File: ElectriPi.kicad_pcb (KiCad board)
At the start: 2 copper layers, 65 x 56 mm, 59 parts, among them IC2 TPS51397ARJER, J1 282837-2, J3 JST XH 01x02, J4 282837-2, J6 Raspberry_Pi_2_3, Q1 SiA471DJ, U1 LM73100, U2 COOLING, U3 TVS0500DRV, U4 LM73100

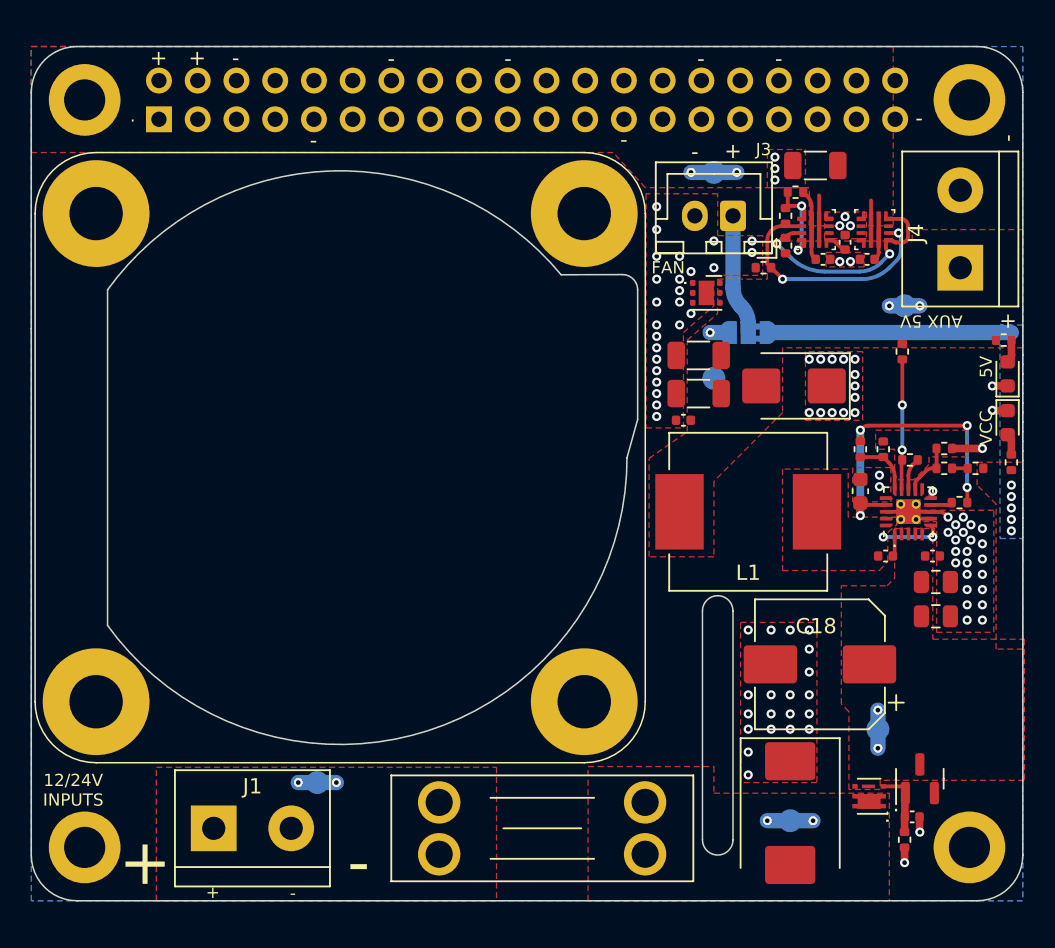
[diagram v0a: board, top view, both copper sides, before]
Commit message: Change to 40 pin passthrough header
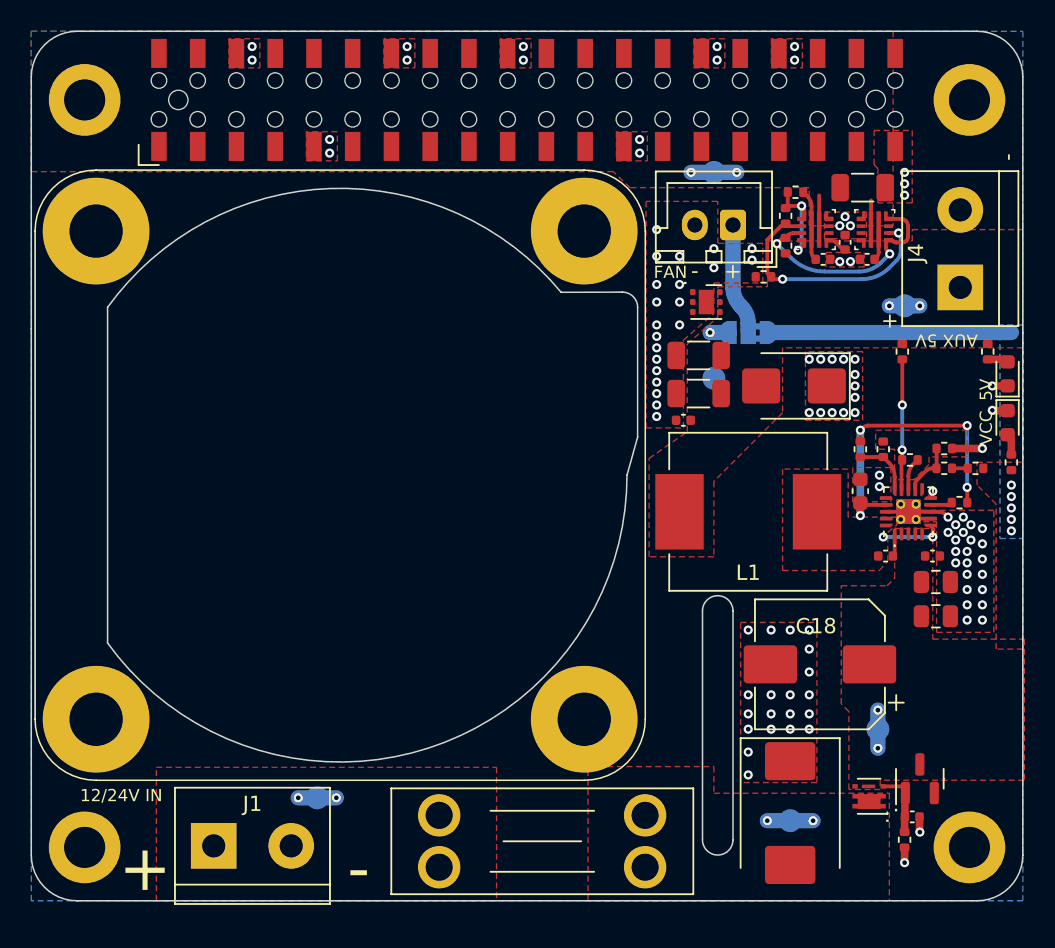
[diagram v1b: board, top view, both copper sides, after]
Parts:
- J6: value Raspberry_Pi_2_3 -> Raspberry_Pi_Header; footprint Connector_PinSocket_2.54mm:PinSocket_2x20_P2.54mm_Vertical -> PI_GPIO_PASSTHROUGH:SSM-120-_-DV-BE; moved to F.Cu
- moved C12 3.42 mm to (139.8, 62.5), turned to 0 degrees
- moved R6 1.29 mm to (147.9, 73.2), turned to 90 degrees
- moved J4 1.29 mm to (146.2, 69.0)
- moved J1 1.15 mm to (97.2, 105.7)
- moved U2 1.15 mm to (105.5, 81.3)
- moved TP2 1.00 mm to (104.0, 102.5)
- moved F1 0.85 mm to (112.0, 103.7)
- moved J3 0.60 mm to (131.2, 65.0)
- moved R10 0.60 mm to (133.2, 68.3)
- moved U3 0.60 mm to (129.5, 70.0)
- turned J6 to 90 degrees
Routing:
- net Net-(J3-Pin_1): track 7.91 -> 7.31 mm
- net GND: vias 97 -> 107
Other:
- board size 65 x 56 mm -> 65 x 57 mm
- board text added: "12/24V IN"
- board text removed: "12/24V INPUTS"

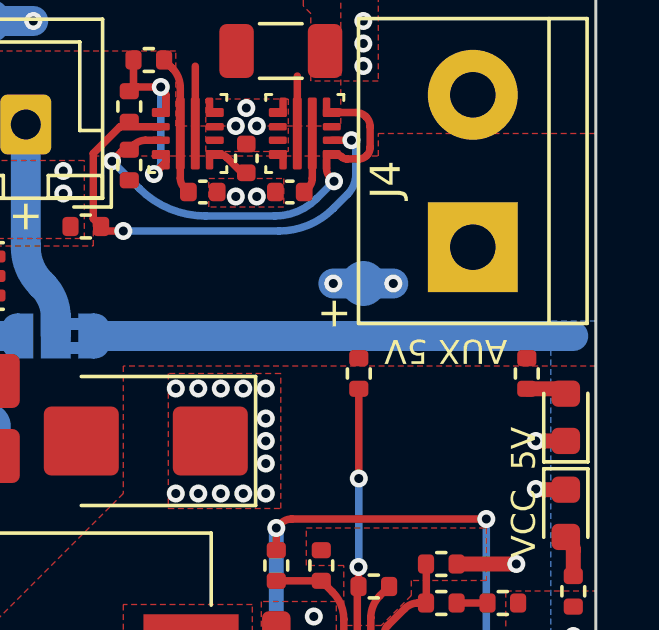
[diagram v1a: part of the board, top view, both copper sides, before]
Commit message: Change silk and test point position. Update manufacturing outputs. Header product number not yet specified
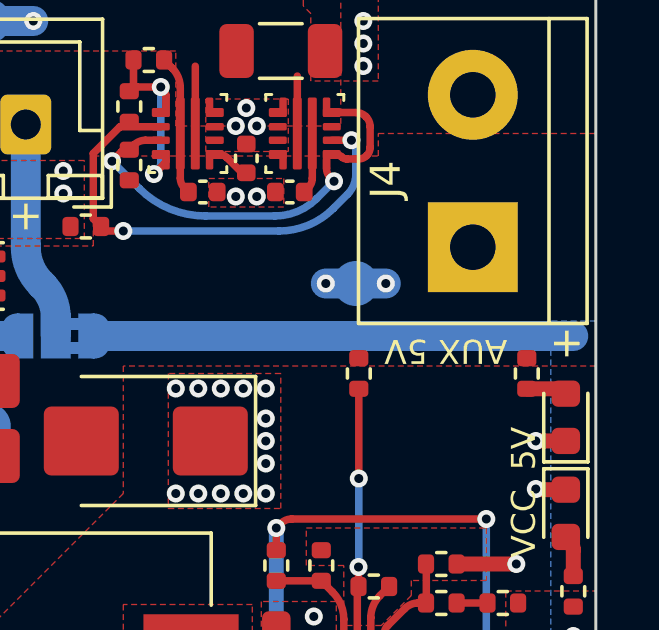
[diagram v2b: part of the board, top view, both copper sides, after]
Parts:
- moved TP1 0.25 mm to (142.2, 70.2)
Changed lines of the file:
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@@
 		(pad_to_mask_clearance 0)
 		(allow_soldermask_bridges_in_footprints no)
-		(aux_axis_origin 85.25 53.25)
-		(grid_origin 85.25 53.25)
+		(aux_axis_origin 85.25 52.25)
+		(grid_origin 85.25 52.249996)
 		(pcbplotparams
 			(layerselection 0x00010fe_ffffffff)
@@
 		(tags "capacitor")
 		(property "Reference" "C12"
-			(at 0 -1.85 360)
+			(at 0 -1.85 0)
 			(layer "F.SilkS")
 			(hide yes)
@@
 		)
 		(property "Value" "100uF"
-			(at 0 1.85 360)
+			(at 0 1.85 0)
 			(layer "F.Fab")
 			(effects
@@
 		)
 		(property "Footprint" "Capacitor_SMD:C_1206_3216Metric"
-			(at 0 0 360)
+			(at 0 0 0)
 			(layer "F.Fab")
 			(hide yes)
@@
 		)
 		(property "Datasheet" ""
-			(at 0 0 360)
+			(at 0 0 0)
 			(layer "F.Fab")
 			(hide yes)
@@
 		)
 		(property "Description" ""
-			(at 0 0 360)
+			(at 0 0 0)
 			(layer "F.Fab")
 			(hide yes)
@@
 		)
 		(property "DigiKey" "490-GRM31CR61A107MEA8KTR-ND"
-			(at 273.3 122.1 360)
+			(at 273.3 122.1 0)
 			(layer "F.Fab")
 			(hide yes)
@@
 		)
 		(property "LCSC" "C312983"
-			(at 273.3 122.1 360)
+			(at 273.3 122.1 0)
 			(layer "F.Fab")
 			(hide yes)
@@
 		)
 		(property "Mouser" "81-GRM31CR61A107MA8L"
-			(at 273.3 122.1 360)
+			(at 273.3 122.1 0)
 			(layer "F.Fab")
 			(hide yes)
@@
 		)
 		(fp_text user "${REFERENCE}"
-			(at 0 0 360)
+			(at 0 0 0)
 			(layer "F.Fab")
 			(effects
@@
 		)
 		(fp_text user "${REFERENCE}"
-			(at 1.27 24.13 360)
+			(at 1.27 24.13 0)
 			(layer "F.Fab")
 			(effects
@@
 		(tags "resistor")
 		(property "Reference" "R6"
-			(at 1.6 0.35 360)
+			(at 1.6 0.35 0)
 			(layer "F.SilkS")
 			(hide yes)
@@
 	(footprint "TestPoint:TestPoint_Pad_D1.5mm"
 		(layer "B.Cu")
-		(at 142.5 70.25)
+		(at 142.25 70.25)
 		(descr "SMD pad as test Point, diameter 1.5mm")
 		(tags "test point SMD pad")
@@
 	)
 	(gr_text "+"
-		(at 141.5 71.25 90)
+		(at 149.25 72.25 90)
 		(layer "F.SilkS")
 		(effects
@@
 	)
 	(via
-		(at 143.5 70.25)
+		(at 143.25 70.25)
 		(size 0.6)
 		(drill 0.3)
@@
 	)
 	(via
-		(at 141.5 70.25)
+		(at 141.25 70.25)
 		(size 0.6)
 		(drill 0.3)
@@
 	)
 	(segment
-		(start 141.5 70.25)
-		(end 143.5 70.25)
+		(start 141.25 70.25)
+		(end 143.25 70.25)
 		(width 1)
 		(layer "B.Cu")

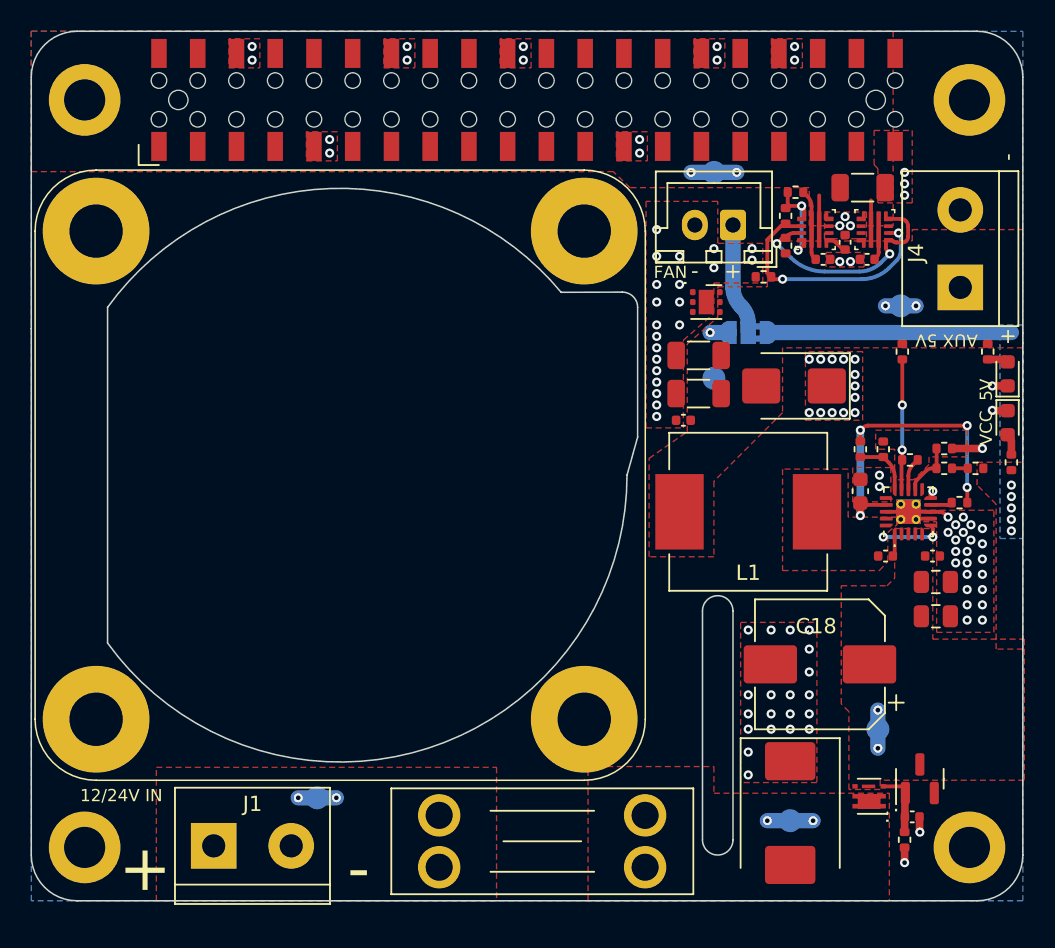
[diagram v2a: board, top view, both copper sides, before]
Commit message: V1.1 Updates
Moved status LEDs away from PCB edge.
Moved and modified AUX 5V label.
Changed screw terminals to JST XH.
Added SMD Header LCSC number.
Added 5mm silkscreen for QR Code
Removed silkscreen border for 4010 fan.
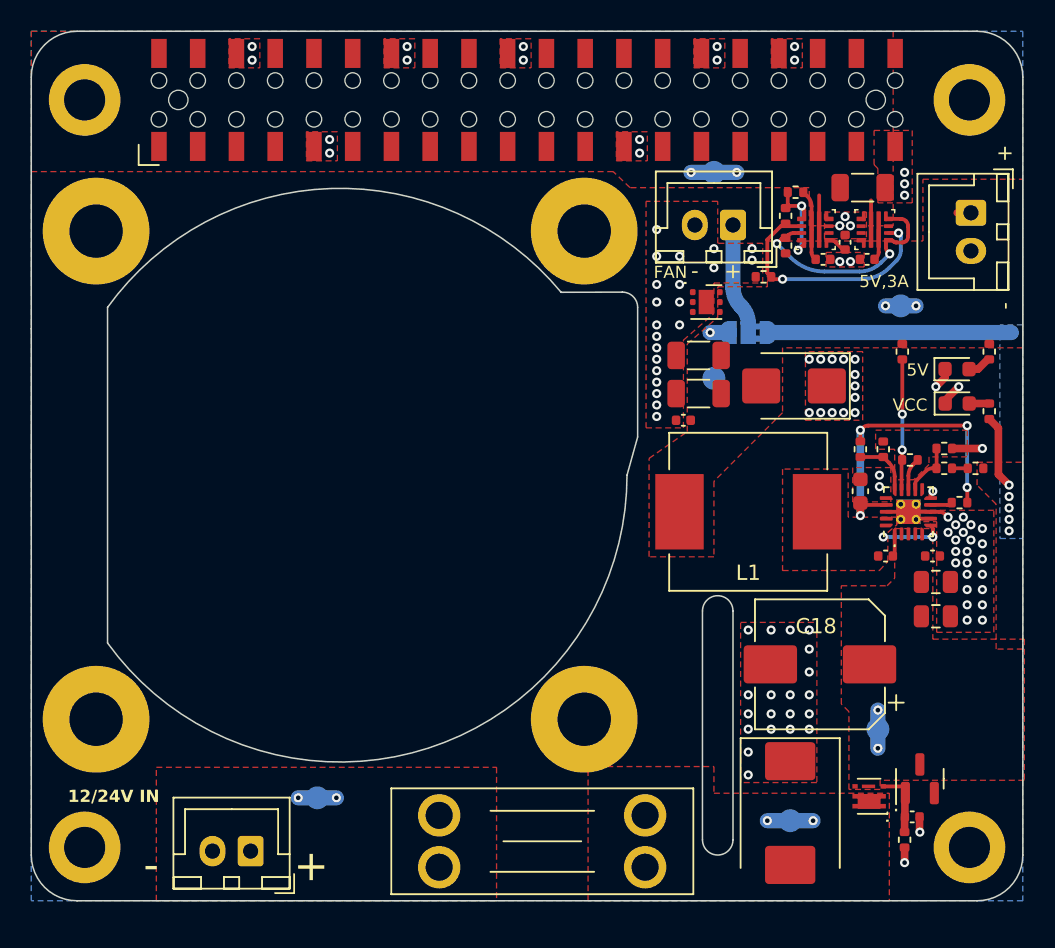
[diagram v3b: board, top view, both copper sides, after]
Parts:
- J1, J4: value 282837-2 -> JST XH 01x02; footprint TerminalBlock:TerminalBlock_bornier-2_P5.08mm -> Connector_JST:JST_XH_B2B-XH-A_1x02_P2.50mm_Vertical
- moved J4 4.94 mm to (146.8, 64.1), turned to -90 degrees
- moved R8 3.65 mm to (148.1, 77.2)
- moved D5 3.53 mm to (145.9, 76.6), turned to 0 degrees
- moved D3 3.33 mm to (145.9, 74.4), turned to 0 degrees
- moved J1 2.44 mm to (99.6, 106.0), turned to 180 degrees
- moved G*** 0.92 mm to (139.7, 89.2)
- moved R6 0.10 mm to (148.1, 73.2)
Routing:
- net Vin: track 18.4 -> 23.3 mm
- net +5V: track 9.91 -> 10.8 mm
- net GND: track 14.3 -> 15.1 mm
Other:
- board text added: "5V,3A"
- board text added: "ElectriPi V1.1"
- board text removed: "AUX 5V"

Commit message: Corrected Version Number on Silk
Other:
- board text added: "ElectriPi V3.2"
- board text removed: "ElectriPi V1.1"
- board text removed: "V3.1"
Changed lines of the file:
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@@
 		)
 	)
-	(gr_text "V3.1"
-		(at 128 97.5 270)
+	(gr_text "ElectriPi V3.2"
+		(at 87.75 80.999996 270)
 		(layer "B.SilkS")
 		(effects
-			(font
-				(size 1 1)
-				(thickness 0.15)
-			)
-			(justify mirror)
-		)
-	)
-	(gr_text "ElectriPi V1.1"
-		(at 87.75 80.999996 -90)
-		(layer "B.SilkS")
-		(effects
